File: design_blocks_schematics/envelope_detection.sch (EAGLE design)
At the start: 13 parts

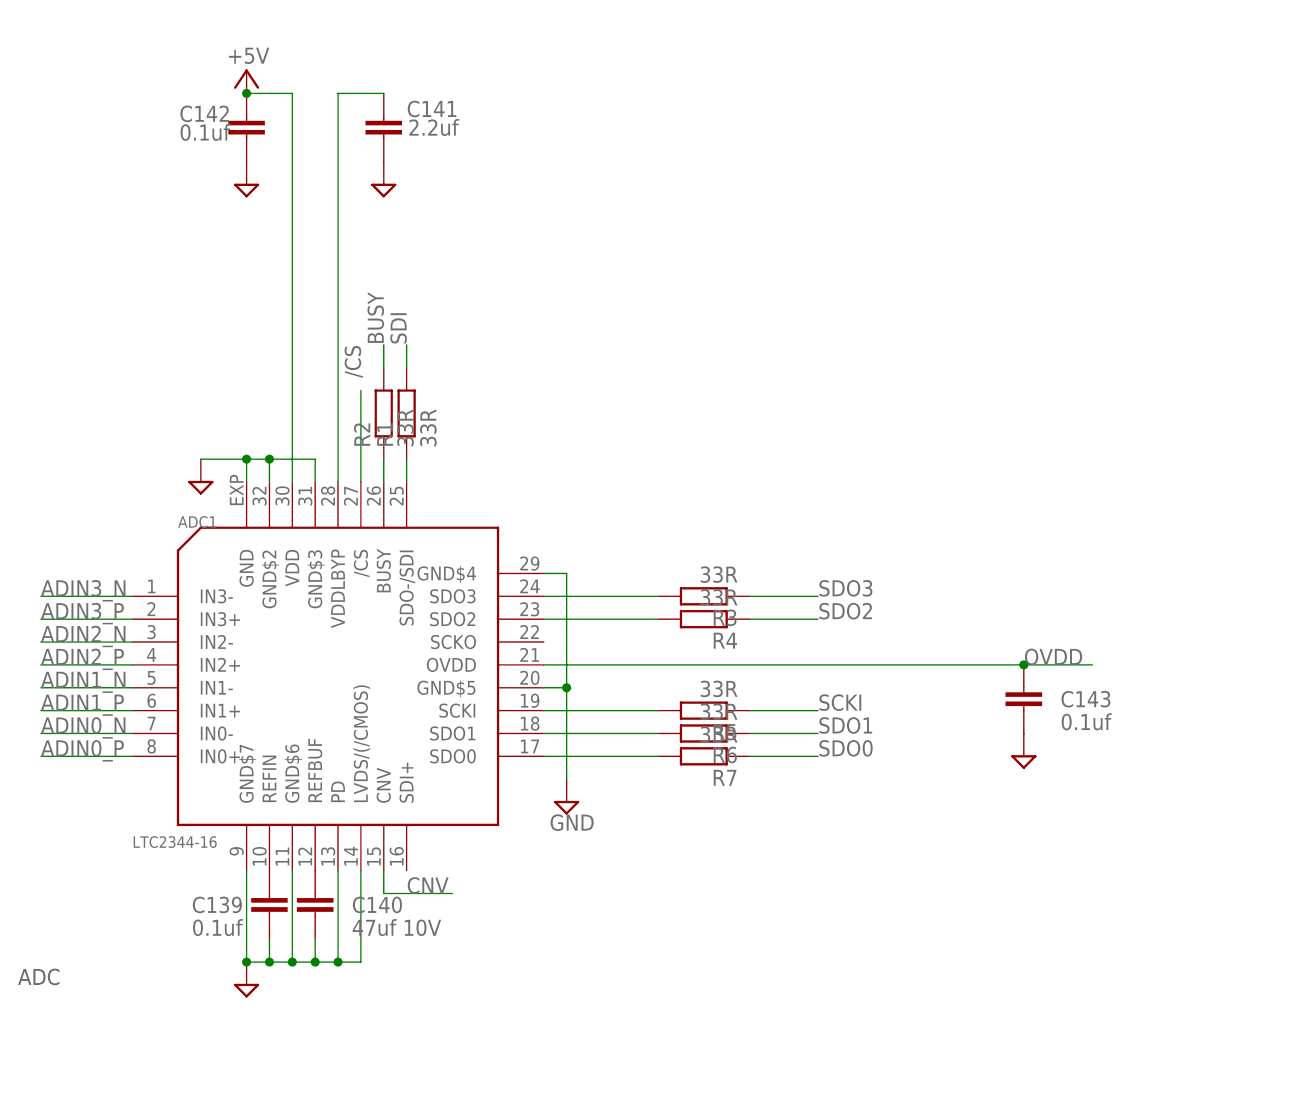
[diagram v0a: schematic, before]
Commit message: updated board size of dbl added envelope detection: - simulation - design block
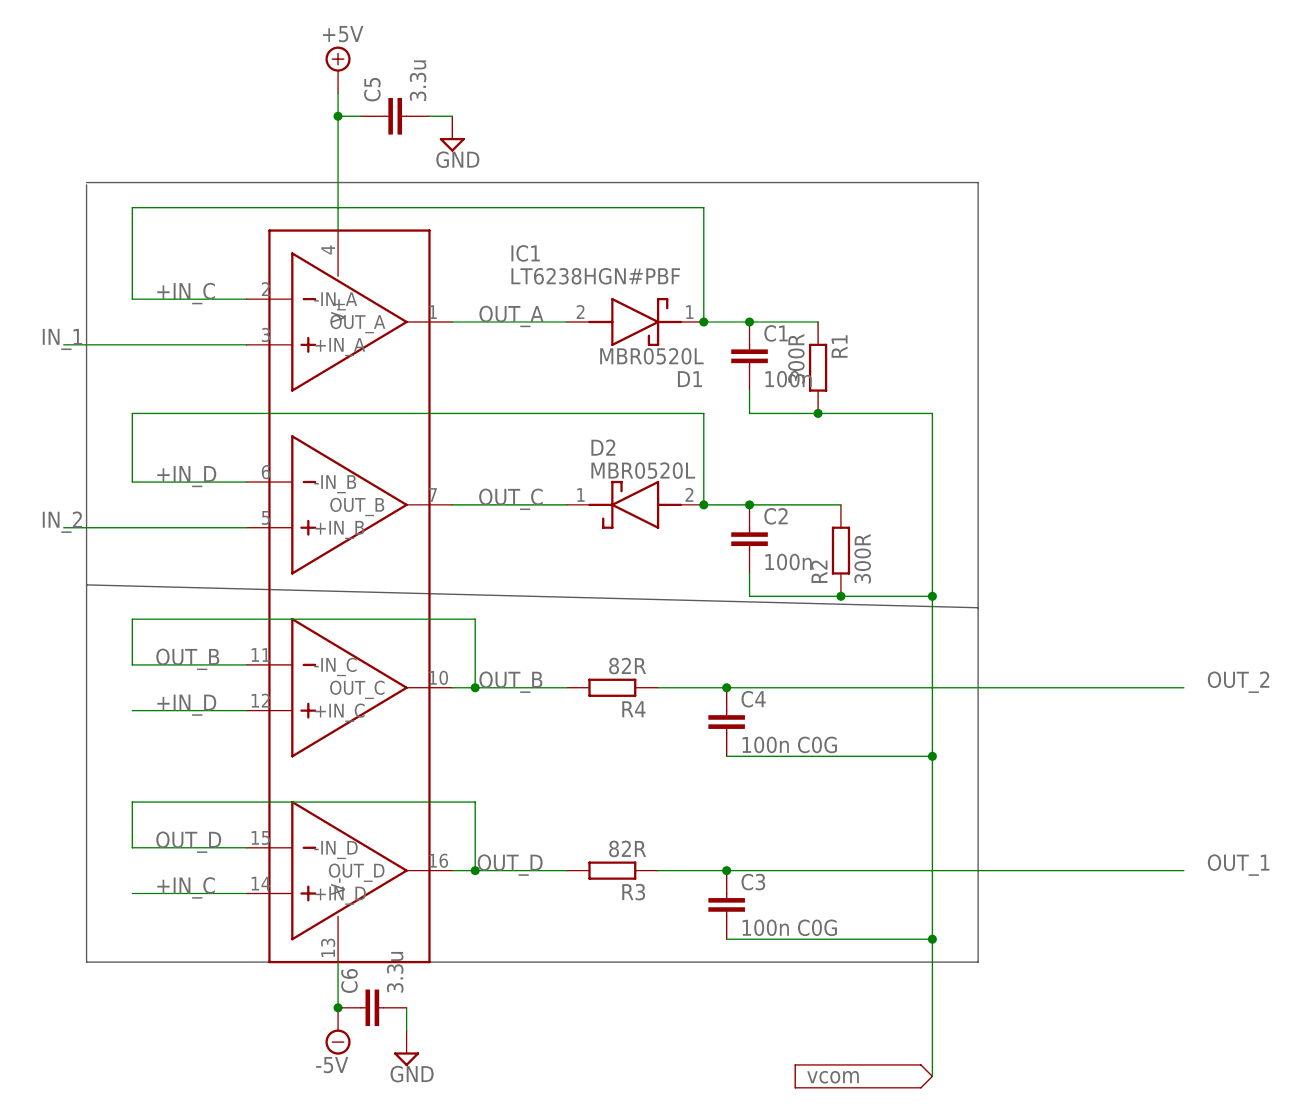
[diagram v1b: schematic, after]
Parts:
- removed ADC1: LTC2344-16, wouter:LTC2344-16
- removed C139, C142, C143: 0.1uf, rcl:C-EUC0402
- removed C140: 47uf 10V, rcl:C-EUC1210
- removed R5, R6, R7: 33R, rcl:R-EU_R0402
- added C1, C2: 100n, rcl:C-EUC0603
- added C3, C4: 100n C0G, rcl:C-EUC1206
- added C6: 3.3u, rcl:C-EUC0402
- added D1, D2: MBR0520L, wouter:MBR0520L
- added IC1: LT6238HGN#PBF, wouter:LT6238HGN#PBF
- C5: value 2.2uf -> 3.3u
- R1, R2: value 33R -> 300R; device rcl:R-EU_R0402 -> rcl:R-EU_M0805
- R3, R4: value 33R -> 82R; device rcl:R-EU_R0402 -> rcl:R-EU_M0805
- renumbered C141 to C5
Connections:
- removed net /CS: ADC1./CS
- removed net ADIN0_N: ADC1.IN0-
- removed net ADIN0_P: ADC1.IN0+
- removed net ADIN1_N: ADC1.IN1-
- removed net ADIN1_P: ADC1.IN1+
- removed net ADIN2_N: ADC1.IN2-
- removed net ADIN2_P: ADC1.IN2+
- removed net ADIN3_N: ADC1.IN3-
- removed net ADIN3_P: ADC1.IN3+
- removed net BUSY: R2.2
- removed net CNV: ADC1.CNV
- removed net N$1: ADC1.SDO3, R3.2
- removed net N$2: ADC1.SDO2, R4.2
- removed net N$3: ADC1.SCKI, R5.2
- removed net N$4: ADC1.SDO1, R6.2
- removed net N$5: ADC1.SDO0, R7.2
- removed net N$81: ADC1.REFIN, C139.1
- removed net N$82: ADC1.REFBUF, C140.1
- removed net N$83: ADC1.VDDLBYP, C5.1
- removed net N1: ADC1.BUSY, R2.1
- removed net N2: ADC1.SDO-/SDI, R1.1
- removed net OVDD: ADC1.OVDD, C143.1
- removed net SCKI: R5.1
- removed net SDI: R1.2
- removed net SDO0: R7.1
- removed net SDO1: R6.1
- removed net SDO2: R4.1
- removed net SDO3: R3.1
- new net +IN_C: C1.1, D1.K, IC1.+IN_D, IC1.-IN_A, R1.1
- new net +IN_D: C2.1, D2.A, IC1.+IN_C, IC1.-IN_B, R2.2
- new net -5V: C6.1, IC1.V-
- new net IN_1: IC1.+IN_A
- new net IN_2: IC1.+IN_B
- new net OUT_1: C3.1, R3.1
- new net OUT_2: C4.1, R4.1
- new net OUT_A: D1.A, IC1.OUT_A
- new net OUT_B: IC1.-IN_C, IC1.OUT_C, R4.2
- new net OUT_C: D2.K, IC1.OUT_B
- new net OUT_D: IC1.-IN_D, IC1.OUT_D, R3.2
- new net VCOM: C1.2, C2.2, C3.2, C4.2, R1.2, R2.1
- net +5V: now also C5.1, IC1.V+; no longer ADC1.VDD, C142.1
- net GND: now also C6.2; no longer ADC1.GND, ADC1.GND$2, ADC1.GND$3, ADC1.GND$4, ADC1.GND$5, ADC1.GND$6, ADC1.GND$7, ADC1.LVDS/(/CMOS), ADC1.PD, C139.2, C140.2, C142.2, C143.2
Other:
- note removed: "ADC"
- moved on the sheet: R1, R2, R3, R4
